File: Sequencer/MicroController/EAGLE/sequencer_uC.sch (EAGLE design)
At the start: 1 part

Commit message: First draft of schematic
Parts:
- added C1: 100uF, rcl:CPOL-USE5-8.5
- added C2: 4.7uF, rcl:C-EU050-024X044
- added C3, C4: 22pF, rcl:C-EU050-024X044
- added J1: AVR_SPI_PROG_3X2NS, SparkFun-Connectors:AVR_SPI_PROG_3X2NS
- added J2, J3: (no value), SparkFun-Connectors:6_PIN_SERIAL_TARGETLONGPADS
- added J4, J5: (no value), SparkFun-Connectors:I2C_STANDARD
- added JP1, JP2: (no value), jumper:JP1Q
- added L1: 47uH, rcl:L-EU0207/10
- added Q1: 16MHz, special:XTAL/S
- added R1: 10k, rcl:R-US_0309/10
- added R2, R3, R4: 10k, rcl:R-US_0204/7
- added SV1: (no value), con-lstb:MA20-2
- added SV2, SV3, SV4, SV5, SV6: (no value), con-lstb:MA03-2
- added U$1: TER6PIN_VERT, TE6Pin:TER6PIN_VERT
- added V1, V2: 74595N, 74ttl-din:74595N
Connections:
- new net +5V: AT1.VCC, C1.+, C2.1, J1.2, J2.VCC, J3.VCC, J4.2, J5.2, R1.2, R2.2, R3.2, SV1.2, SV1.35, SV1.37, SV1.39, SV1.4, SV1.6, SV6.4, U$1.+5V, V1/+UB.+UB, V2/+UB.+UB
- new net AGND: L1.2, U$1.AGND0, U$1.AGND1
- new net CTS0: AT1.A3, J2.CTS
- new net CTS1: AT1.A2, J3.CTS
- new net DGND: AT1.GND, C1.-, C2.2, J1.6, J2.GND, J3.GND, J4.1, J5.1, L1.1, R4.1, SV1.1, SV1.10, SV1.11, SV1.12, SV1.14, SV1.15, SV1.16, SV1.18, SV1.20, SV1.22, SV1.24, SV1.26, SV1.28, SV1.3, SV1.30, SV1.32, SV1.5, SV1.7, SV1.8, SV6.2, U$1.DGND, V1/-UB.-UB, V2/-UB.-UB
- new net DTR0: AT1.A1, J2.DTR
- new net DTR1: AT1.A0, J3.DTR
- new net EXT0: V11.QH*, V21.SER
- new net EXT1: V21.QH*
- new net IN0: SV2.5, SV2.6, V21.QH
- new net IN1: SV2.3, SV2.4, V21.QG
- new net IN10: SV5.3, SV5.4, V11.QF
- new net IN11: SV5.1, SV5.2, V11.QE
- new net IN12: SV6.5, V11.QD
- new net IN13: SV6.3, V11.QC
- new net IN14: SV6.1, V11.QB
- new net IN15: SV6.6, V11.QA
- new net IN2: SV2.1, SV2.2, V21.QF
- new net IN3: SV3.5, SV3.6, V21.QE
- new net IN4: SV3.3, SV3.4, V21.QD
- new net IN5: SV3.1, SV3.2, V21.QC
- new net IN6: SV4.5, SV4.6, V21.QB
- new net IN7: SV4.3, SV4.4, V21.QA
- new net IN8: SV4.1, SV4.2, V11.QH
- new net IN9: SV5.5, SV5.6, V11.QG
- new net LATCH_IN: AT1.D6, SV1.27
- new net LATCH_OUT: AT1.D9, SV1.19
- new net LATCH_TRIG: AT1.D3, V11.RCK, V21.RCK
- new net MISO: AT1.D12, J1.1
- new net MOSI: AT1.D11, J1.4
- new net N$1: AT1.XTAL1, C3.2
- new net N$2: AT1.XTAL2, C4.2
- new net N$3: C3.1, Q1.2
- new net N$4: C4.1, Q1.1
- new net N$5: JP2.2, SV1.13
- new net N$6: JP1.2, SV1.9
- new net RESET: AT1.RESET, J1.5, R1.1
- new net RXD: AT1.RXD/D0, J2.TXO, J3.TXO
- new net SCK: AT1.D13, J1.3
- new net SCL: AT1.A5, J4.4, J5.4, JP2.1, R2.1
- new net SDA: AT1.A4, J4.3, J5.3, JP1.1, R3.1
- new net SERIAL_IN: AT1.D7, SV1.29
- new net SERIAL_OUT: AT1.D8, SV1.21
- new net SERIAL_TRIG: AT1.D4, V11.SER
- new net SHIFT_IN: AT1.D5, SV1.25
- new net SHIFT_OUT: AT1.D10, SV1.17
- new net SHIFT_TRIG: AT1.D2, V11.SRCK, V21.SRCK
- new net TXD: AT1.TXD/D1, J2.RXI, J3.RXI
- new net ~EN: R4.2, V11.!G, V21.!G
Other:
- note added: "ATMEGA328p"
- note added: "Extra Trigger Output"
- note added: "Instrument Trigger"
- note added: "Might find a use for these"
- note added: "Power Input"
- note added: "Programmer Input"
- note added: "Serial Expansion"
- note added: "Use 4.7k on i2c slave devices"

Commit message: Finished board.
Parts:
- added C5: 100n, rcl:C-EU050-024X044
- added JP3: (no value), jumper:JP1Q
- R1: device rcl:R-US_0309/10 -> resistor:R-US_0204/7
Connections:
- new net N$7: C5.1, JP3.2
- net DTR1: now also JP3.1
- net RESET: now also C5.2
- net SERIAL_TRIG: now also AT1.D2; no longer AT1.D4
- net SHIFT_TRIG: now also AT1.D4; no longer AT1.D2
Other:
- note added: "Use as Programmer"
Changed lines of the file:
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@@
 <part name="P+2" library="supply1" library_urn="urn:adsk.eagle:library:371" deviceset="+5V" device=""/>
 <part name="SUPPLY3" library="supply2" library_urn="urn:adsk.eagle:library:372" deviceset="DGND" device=""/>
-<part name="R1" library="rcl" library_urn="urn:adsk.eagle:library:334" deviceset="R-US_" device="0309/10" package3d_urn="urn:adsk.eagle:package:23567/2" value="10k"/>
+<part name="R1" library="resistor" library_urn="urn:adsk.eagle:library:348" deviceset="R-US_" device="0204/7" package3d_urn="urn:adsk.eagle:package:23498/1" value="10k"/>
 <part name="P+3" library="supply1" library_urn="urn:adsk.eagle:library:371" deviceset="+5V" device=""/>
 <part name="J2" library="SparkFun-Connectors" library_urn="urn:adsk.eagle:library:513" deviceset="6_PIN_SERIAL_TARGET" device="LONGPADS" package3d_urn="urn:adsk.eagle:package:37991/1"/>
@@
 <part name="R4" library="rcl" library_urn="urn:adsk.eagle:library:334" deviceset="R-US_" device="0204/7" package3d_urn="urn:adsk.eagle:package:23498/2" value="10k"/>
 <part name="SUPPLY4" library="supply2" library_urn="urn:adsk.eagle:library:372" deviceset="DGND" device=""/>
+<part name="C5" library="rcl" library_urn="urn:adsk.eagle:library:334" deviceset="C-EU" device="050-024X044" package3d_urn="urn:adsk.eagle:package:23643/1" value="100n"/>
+<part name="JP3" library="jumper" library_urn="urn:adsk.eagle:library:252" deviceset="JP1Q" device="" package3d_urn="urn:adsk.eagle:package:15455/1"/>
 </parts>
 <sheets>
@@
 <text x="182.88" y="147.32" size="1.778" layer="91">Use 4.7k on i2c slave devices</text>
 <text x="228.6" y="116.84" size="1.778" layer="91" rot="R180">Might find a use for these</text>
+<text x="165.1" y="96.52" size="1.778" layer="91">Use as
+Programmer</text>
 </plain>
 <instances>
@@
 <instance part="SUPPLY4" gate="G$1" x="12.7" y="7.62" smashed="yes">
 <attribute name="VALUE" x="10.033" y="4.445" size="1.778" layer="96"/>
+</instance>
+<instance part="C5" gate="G$1" x="182.88" y="99.06" smashed="yes">
+<attribute name="NAME" x="184.404" y="99.441" size="1.778" layer="95"/>
+<attribute name="VALUE" x="184.404" y="94.361" size="1.778" layer="96"/>
+</instance>
+<instance part="JP3" gate="A" x="172.72" y="104.14" smashed="yes" rot="R270">
+<attribute name="NAME" x="167.64" y="106.68" size="1.778" layer="95"/>
+<attribute name="VALUE" x="167.64" y="99.695" size="1.778" layer="96"/>
 </instance>
 </instances>
@@
 <label x="106.68" y="137.16" size="1.778" layer="95"/>
 </segment>
+<segment>
+<pinref part="C5" gate="G$1" pin="2"/>
+<wire x1="182.88" y1="93.98" x2="182.88" y2="91.44" width="0.1524" layer="91"/>
+<wire x1="182.88" y1="91.44" x2="187.96" y2="91.44" width="0.1524" layer="91"/>
+<label x="187.96" y="91.44" size="1.778" layer="95"/>
+</segment>
 </net>
 <net name="SCK" class="0">
@@
 <net name="SHIFT_TRIG" class="0">
 <segment>
+<pinref part="V2" gate="1" pin="SRCK"/>
+<wire x1="116.84" y1="17.78" x2="116.84" y2="12.7" width="0.1524" layer="91"/>
+<label x="116.84" y="12.7" size="1.778" layer="95"/>
+</segment>
+<segment>
+<pinref part="V1" gate="1" pin="SRCK"/>
+<wire x1="33.02" y1="25.4" x2="33.02" y2="17.78" width="0.1524" layer="91"/>
+<label x="33.02" y="17.78" size="1.778" layer="95"/>
+</segment>
+<segment>
+<pinref part="AT1" gate="G$1" pin="D4"/>
+<label x="93.98" y="111.76" size="1.778" layer="95"/>
+<wire x1="119.38" y1="111.76" x2="111.76" y2="111.76" width="0.1524" layer="91"/>
+</segment>
+</net>
+<net name="LATCH_TRIG" class="0">
+<segment>
+<pinref part="V2" gate="1" pin="RCK"/>
+<wire x1="101.6" y1="17.78" x2="101.6" y2="10.16" width="0.1524" layer="91"/>
+<label x="101.6" y="10.16" size="1.778" layer="95"/>
+</segment>
+<segment>
+<pinref part="V1" gate="1" pin="RCK"/>
+<wire x1="17.78" y1="25.4" x2="17.78" y2="12.7" width="0.1524" layer="91"/>
+<label x="17.78" y="12.7" size="1.778" layer="95"/>
+</segment>
+<segment>
+<pinref part="AT1" gate="G$1" pin="D3"/>
+<wire x1="119.38" y1="116.84" x2="116.84" y2="116.84" width="0.1524" layer="91"/>
+<label x="93.98" y="114.3" size="1.778" layer="95"/>
+<wire x1="116.84" y1="116.84" x2="116.84" y2="114.3" width="0.1524" layer="91"/>
+<wire x1="116.84" y1="114.3" x2="111.76" y2="114.3" width="0.1524" layer="91"/>
+</segment>
+</net>
+<net name="SERIAL_TRIG" class="0">
+<segment>
+<pinref part="V1" gate="1" pin="SER"/>
+<wire x1="40.64" y1="25.4" x2="40.64" y2="22.86" width="0.1524" layer="91"/>
+<label x="40.64" y="22.86" size="1.778" layer="95"/>
+</segment>
+<segment>
 <pinref part="AT1" gate="G$1" pin="D2"/>
 <wire x1="119.38" y1="121.92" x2="114.3" y2="121.92" width="0.1524" layer="91"/>
@@
 <wire x1="114.3" y1="121.92" x2="114.3" y2="116.84" width="0.1524" layer="91"/>
 <wire x1="114.3" y1="116.84" x2="111.76" y2="116.84" width="0.1524" layer="91"/>
-</segment>
-<segment>
-<pinref part="V2" gate="1" pin="SRCK"/>
-<wire x1="116.84" y1="17.78" x2="116.84" y2="12.7" width="0.1524" layer="91"/>
-<label x="116.84" y="12.7" size="1.778" layer="95"/>
-</segment>
-<segment>
-<pinref part="V1" gate="1" pin="SRCK"/>
-<wire x1="33.02" y1="25.4" x2="33.02" y2="17.78" width="0.1524" layer="91"/>
-<label x="33.02" y="17.78" size="1.778" layer="95"/>
-</segment>
-</net>
-<net name="LATCH_TRIG" class="0">
-<segment>
-<pinref part="AT1" gate="G$1" pin="D3"/>
-<wire x1="119.38" y1="116.84" x2="116.84" y2="116.84" width="0.1524" layer="91"/>
-<label x="93.98" y="114.3" size="1.778" layer="95"/>
-<wire x1="116.84" y1="116.84" x2="116.84" y2="114.3" width="0.1524" layer="91"/>
-<wire x1="116.84" y1="114.3" x2="111.76" y2="114.3" width="0.1524" layer="91"/>
-</segment>
-<segment>
-<pinref part="V2" gate="1" pin="RCK"/>
-<wire x1="101.6" y1="17.78" x2="101.6" y2="10.16" width="0.1524" layer="91"/>
-<label x="101.6" y="10.16" size="1.778" layer="95"/>
-</segment>
-<segment>
-<pinref part="V1" gate="1" pin="RCK"/>
-<wire x1="17.78" y1="25.4" x2="17.78" y2="12.7" width="0.1524" layer="91"/>
-<label x="17.78" y="12.7" size="1.778" layer="95"/>
-</segment>
-</net>
-<net name="SERIAL_TRIG" class="0">
-<segment>
-<pinref part="AT1" gate="G$1" pin="D4"/>
-<label x="93.98" y="111.76" size="1.778" layer="95"/>
-<wire x1="119.38" y1="111.76" x2="111.76" y2="111.76" width="0.1524" layer="91"/>
-</segment>
-<segment>
-<pinref part="V1" gate="1" pin="SER"/>
-<wire x1="40.64" y1="25.4" x2="40.64" y2="22.86" width="0.1524" layer="91"/>
-<label x="40.64" y="22.86" size="1.778" layer="95"/>
 </segment>
 </net>
@@
 <segment>
 <pinref part="AT1" gate="G$1" pin="A0"/>
-<wire x1="160.02" y1="111.76" x2="165.1" y2="111.76" width="0.1524" layer="91"/>
+<wire x1="160.02" y1="111.76" x2="162.56" y2="111.76" width="0.1524" layer="91"/>
 <label x="165.1" y="111.76" size="1.778" layer="95"/>
+<wire x1="162.56" y1="111.76" x2="165.1" y2="111.76" width="0.1524" layer="91"/>
+<wire x1="162.56" y1="111.76" x2="162.56" y2="104.14" width="0.1524" layer="91"/>
+<junction x="162.56" y="111.76"/>
+<pinref part="JP3" gate="A" pin="1"/>
+<wire x1="162.56" y1="104.14" x2="165.1" y2="104.14" width="0.1524" layer="91"/>
 </segment>
 <segment>
@@
 </segment>
 </net>
+<net name="N$7" class="0">
+<segment>
+<pinref part="JP3" gate="A" pin="2"/>
+<wire x1="182.88" y1="104.14" x2="180.34" y2="104.14" width="0.1524" layer="91"/>
+<wire x1="182.88" y1="104.14" x2="182.88" y2="101.6" width="0.1524" layer="91"/>
+<pinref part="C5" gate="G$1" pin="1"/>
+</segment>
+</net>

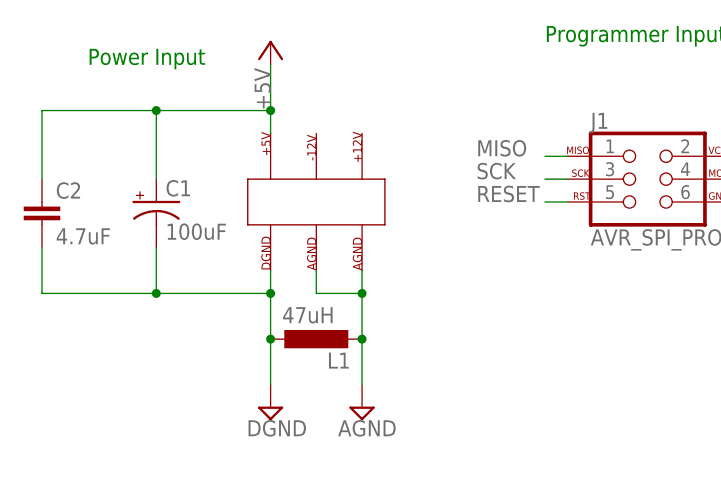
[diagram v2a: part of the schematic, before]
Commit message: fixed TE pinout
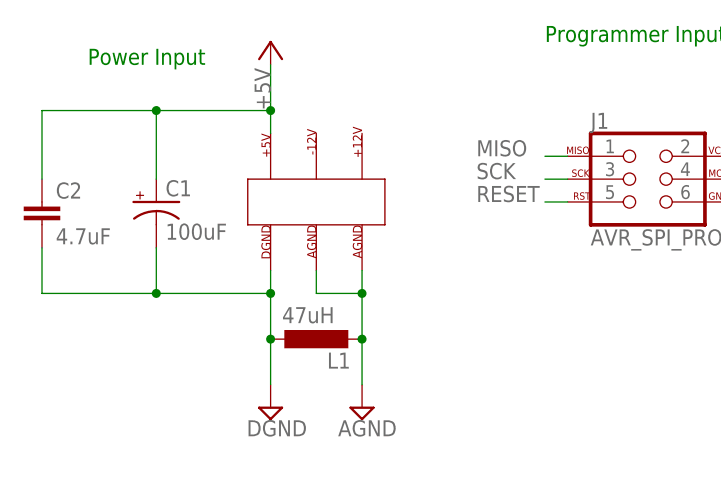
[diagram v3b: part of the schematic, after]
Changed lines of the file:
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@@
 <?xml version="1.0" encoding="utf-8"?>
 <!DOCTYPE eagle SYSTEM "eagle.dtd">
-<eagle version="9.3.1">
+<eagle version="9.2.2">
 <drawing>
 <settings>
@@
 <part name="C2" library="rcl" library_urn="urn:adsk.eagle:library:334" deviceset="C-EU" device="050-024X044" package3d_urn="urn:adsk.eagle:package:23643/1" value="4.7uF"/>
 <part name="SUPPLY2" library="supply2" library_urn="urn:adsk.eagle:library:372" deviceset="AGND" device=""/>
-<part name="L1" library="rcl" library_urn="urn:adsk.eagle:library:334" deviceset="L-EU" device="0207/10" package3d_urn="urn:adsk.eagle:package:23491/2" value="47uH"/>
+<part name="L1" library="rcl" library_urn="urn:adsk.eagle:library:334" deviceset="L-EU" device="0207/10" package3d_urn="urn:adsk.eagle:package:23491/1" value="47uH"/>
 <part name="Q1" library="special" library_urn="urn:adsk.eagle:library:367" deviceset="XTAL/S" device="" package3d_urn="urn:adsk.eagle:package:26647/2" value="16MHz"/>
 <part name="C3" library="rcl" library_urn="urn:adsk.eagle:library:334" deviceset="C-EU" device="050-024X044" package3d_urn="urn:adsk.eagle:package:23643/1" value="22pF"/>
@@
 <part name="P+2" library="supply1" library_urn="urn:adsk.eagle:library:371" deviceset="+5V" device=""/>
 <part name="SUPPLY3" library="supply2" library_urn="urn:adsk.eagle:library:372" deviceset="DGND" device=""/>
-<part name="R1" library="resistor" library_urn="urn:adsk.eagle:library:348" deviceset="R-US_" device="0204/7" package3d_urn="urn:adsk.eagle:package:23498/1" value="10k"/>
+<part name="R1" library="resistor" library_urn="urn:adsk.eagle:library:348" deviceset="R-US_" device="0204/7" package3d_urn="urn:adsk.eagle:package:25945/1" value="10k"/>
 <part name="P+3" library="supply1" library_urn="urn:adsk.eagle:library:371" deviceset="+5V" device=""/>
 <part name="J2" library="SparkFun-Connectors" library_urn="urn:adsk.eagle:library:513" deviceset="6_PIN_SERIAL_TARGET" device="LONGPADS" package3d_urn="urn:adsk.eagle:package:37991/1"/>
@@
 <part name="SV5" library="con-lstb" library_urn="urn:adsk.eagle:library:162" deviceset="MA03-2" device="" package3d_urn="urn:adsk.eagle:package:8334/1"/>
 <part name="SV6" library="con-lstb" library_urn="urn:adsk.eagle:library:162" deviceset="MA03-2" device="" package3d_urn="urn:adsk.eagle:package:8334/1"/>
-<part name="V1" library="74ttl-din" library_urn="urn:adsk.eagle:library:84" deviceset="74*595" device="N" package3d_urn="urn:adsk.eagle:package:922/2"/>
-<part name="V2" library="74ttl-din" library_urn="urn:adsk.eagle:library:84" deviceset="74*595" device="N" package3d_urn="urn:adsk.eagle:package:922/2"/>
+<part name="V1" library="74ttl-din" library_urn="urn:adsk.eagle:library:84" deviceset="74*595" device="N" package3d_urn="urn:adsk.eagle:package:1462/1"/>
+<part name="V2" library="74ttl-din" library_urn="urn:adsk.eagle:library:84" deviceset="74*595" device="N" package3d_urn="urn:adsk.eagle:package:1462/1"/>
 <part name="SUPPLY6" library="supply2" library_urn="urn:adsk.eagle:library:372" deviceset="DGND" device=""/>
 <part name="P+6" library="supply1" library_urn="urn:adsk.eagle:library:371" deviceset="+5V" device=""/>
 <part name="SUPPLY7" library="supply2" library_urn="urn:adsk.eagle:library:372" deviceset="DGND" device=""/>
 <part name="P+7" library="supply1" library_urn="urn:adsk.eagle:library:371" deviceset="+5V" device=""/>
-<part name="R2" library="rcl" library_urn="urn:adsk.eagle:library:334" deviceset="R-US_" device="0204/7" package3d_urn="urn:adsk.eagle:package:23498/2" value="10k"/>
-<part name="R3" library="rcl" library_urn="urn:adsk.eagle:library:334" deviceset="R-US_" device="0204/7" package3d_urn="urn:adsk.eagle:package:23498/2" value="10k"/>
+<part name="R2" library="rcl" library_urn="urn:adsk.eagle:library:334" deviceset="R-US_" device="0204/7" package3d_urn="urn:adsk.eagle:package:23498/1" value="10k"/>
+<part name="R3" library="rcl" library_urn="urn:adsk.eagle:library:334" deviceset="R-US_" device="0204/7" package3d_urn="urn:adsk.eagle:package:23498/1" value="10k"/>
 <part name="P+4" library="supply1" library_urn="urn:adsk.eagle:library:371" deviceset="+5V" device=""/>
 <part name="P+5" library="supply1" library_urn="urn:adsk.eagle:library:371" deviceset="+5V" device=""/>
 <part name="JP1" library="jumper" library_urn="urn:adsk.eagle:library:252" deviceset="JP1Q" device="" package3d_urn="urn:adsk.eagle:package:15455/1"/>
 <part name="JP2" library="jumper" library_urn="urn:adsk.eagle:library:252" deviceset="JP1Q" device="" package3d_urn="urn:adsk.eagle:package:15455/1"/>
-<part name="R4" library="rcl" library_urn="urn:adsk.eagle:library:334" deviceset="R-US_" device="0204/7" package3d_urn="urn:adsk.eagle:package:23498/2" value="10k"/>
+<part name="R4" library="rcl" library_urn="urn:adsk.eagle:library:334" deviceset="R-US_" device="0204/7" package3d_urn="urn:adsk.eagle:package:23498/1" value="10k"/>
 <part name="SUPPLY4" library="supply2" library_urn="urn:adsk.eagle:library:372" deviceset="DGND" device=""/>
 <part name="C5" library="rcl" library_urn="urn:adsk.eagle:library:334" deviceset="C-EU" device="050-024X044" package3d_urn="urn:adsk.eagle:package:23643/1" value="100n"/>
@@
 </instance>
 <instance part="AT1" gate="G$1" x="139.7" y="104.14" smashed="yes"/>
-<instance part="U$1" gate="G$1" x="40.64" y="187.96" smashed="yes"/>
+<instance part="U$1" gate="G$1" x="40.64" y="187.96" smashed="yes" rot="MR180"/>
 <instance part="P+1" gate="1" x="35.56" y="205.74" smashed="yes">
 <attribute name="VALUE" x="35.56" y="198.12" size="1.778" layer="96" rot="R90"/>
@@
 <net name="+5V" class="0">
 <segment>
-<pinref part="U$1" gate="G$1" pin="+5V"/>
-<wire x1="35.56" y1="195.58" x2="35.56" y2="198.12" width="0.1524" layer="91"/>
 <pinref part="P+1" gate="1" pin="+5V"/>
 <pinref part="C1" gate="G$1" pin="+"/>
@@
 <wire x1="22.86" y1="190.5" x2="22.86" y2="198.12" width="0.1524" layer="91"/>
 <wire x1="22.86" y1="198.12" x2="35.56" y2="198.12" width="0.1524" layer="91"/>
-<junction x="35.56" y="198.12"/>
 <pinref part="C2" gate="G$1" pin="1"/>
 <wire x1="10.16" y1="190.5" x2="10.16" y2="198.12" width="0.1524" layer="91"/>
 <wire x1="10.16" y1="198.12" x2="22.86" y2="198.12" width="0.1524" layer="91"/>
 <junction x="22.86" y="198.12"/>
+<pinref part="U$1" gate="G$1" pin="+5V"/>
+<wire x1="35.56" y1="198.12" x2="35.56" y2="195.58" width="0.1524" layer="91"/>
+<junction x="35.56" y="198.12"/>
 </segment>
 <segment>
@@
 <net name="DGND" class="0">
 <segment>
-<pinref part="U$1" gate="G$1" pin="DGND"/>
-<wire x1="35.56" y1="180.34" x2="35.56" y2="177.8" width="0.1524" layer="91"/>
 <pinref part="SUPPLY1" gate="G$1" pin="DGND"/>
 <pinref part="C1" gate="G$1" pin="-"/>
@@
 <wire x1="22.86" y1="182.88" x2="22.86" y2="177.8" width="0.1524" layer="91"/>
 <wire x1="22.86" y1="177.8" x2="35.56" y2="177.8" width="0.1524" layer="91"/>
-<junction x="35.56" y="177.8"/>
 <pinref part="C2" gate="G$1" pin="2"/>
 <wire x1="10.16" y1="182.88" x2="10.16" y2="177.8" width="0.1524" layer="91"/>
@@
 <pinref part="L1" gate="G$1" pin="1"/>
 <junction x="35.56" y="172.72"/>
+<pinref part="U$1" gate="G$1" pin="DGND"/>
+<wire x1="35.56" y1="180.34" x2="35.56" y2="177.8" width="0.1524" layer="91"/>
+<junction x="35.56" y="177.8"/>
 </segment>
 <segment>
@@
 <net name="AGND" class="0">
 <segment>
-<pinref part="U$1" gate="G$1" pin="AGND1"/>
-<wire x1="45.72" y1="180.34" x2="45.72" y2="177.8" width="0.1524" layer="91"/>
 <wire x1="45.72" y1="177.8" x2="40.64" y2="177.8" width="0.1524" layer="91"/>
-<pinref part="U$1" gate="G$1" pin="AGND0"/>
-<wire x1="40.64" y1="177.8" x2="40.64" y2="180.34" width="0.1524" layer="91"/>
 <wire x1="45.72" y1="177.8" x2="45.72" y2="172.72" width="0.1524" layer="91"/>
-<junction x="45.72" y="177.8"/>
 <pinref part="SUPPLY2" gate="G$1" pin="AGND"/>
 <pinref part="L1" gate="G$1" pin="2"/>
 <wire x1="45.72" y1="172.72" x2="45.72" y2="167.64" width="0.1524" layer="91"/>
 <junction x="45.72" y="172.72"/>
+<pinref part="U$1" gate="G$1" pin="AGND0"/>
+<wire x1="40.64" y1="177.8" x2="40.64" y2="180.34" width="0.1524" layer="91"/>
+<pinref part="U$1" gate="G$1" pin="AGND1"/>
+<wire x1="45.72" y1="177.8" x2="45.72" y2="180.34" width="0.1524" layer="91"/>
+<junction x="45.72" y="177.8"/>
 </segment>
 </net>
